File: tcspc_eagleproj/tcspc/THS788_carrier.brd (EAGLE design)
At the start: 50.8 x 38.1 mm, 46 parts, among them J1 BXE-040-01-F-D-A_BSE, U1 THS788

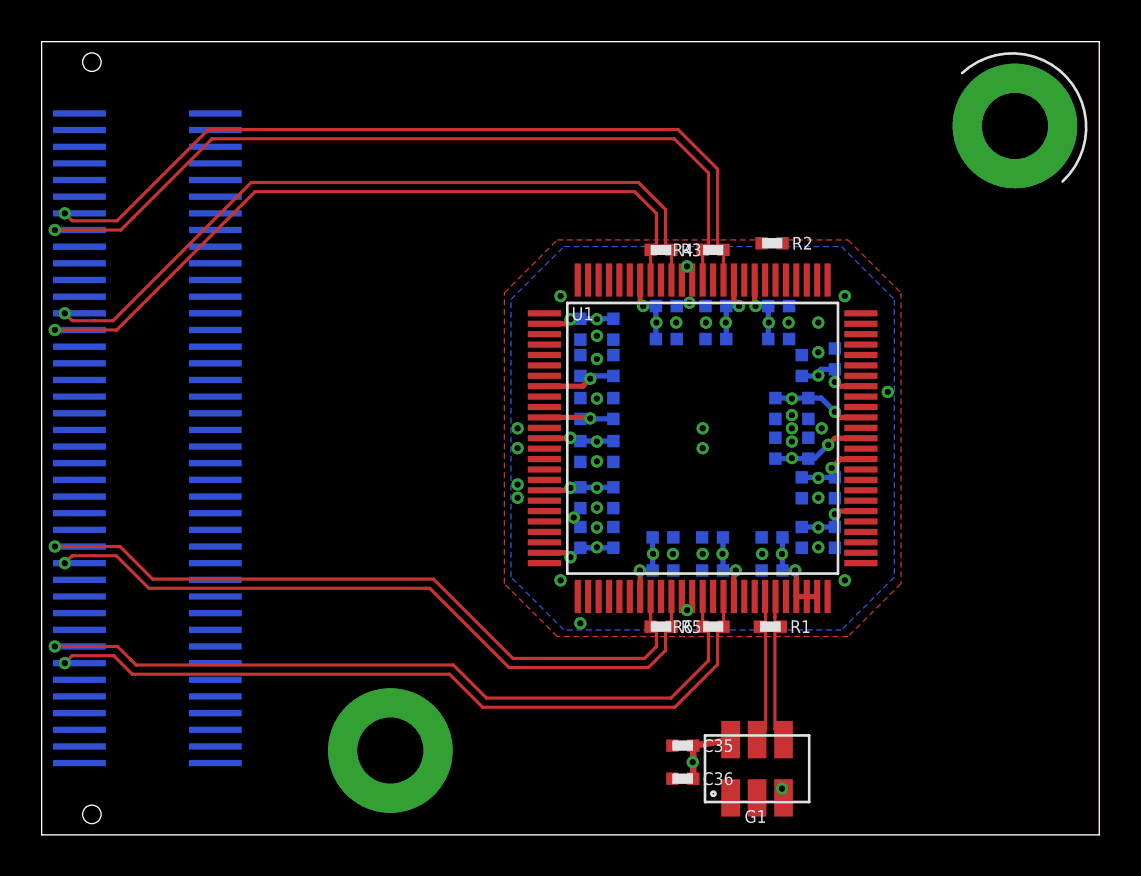
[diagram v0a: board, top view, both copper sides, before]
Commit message: Did a little more work on the THS788 carrier, routed a few more HS diff signals
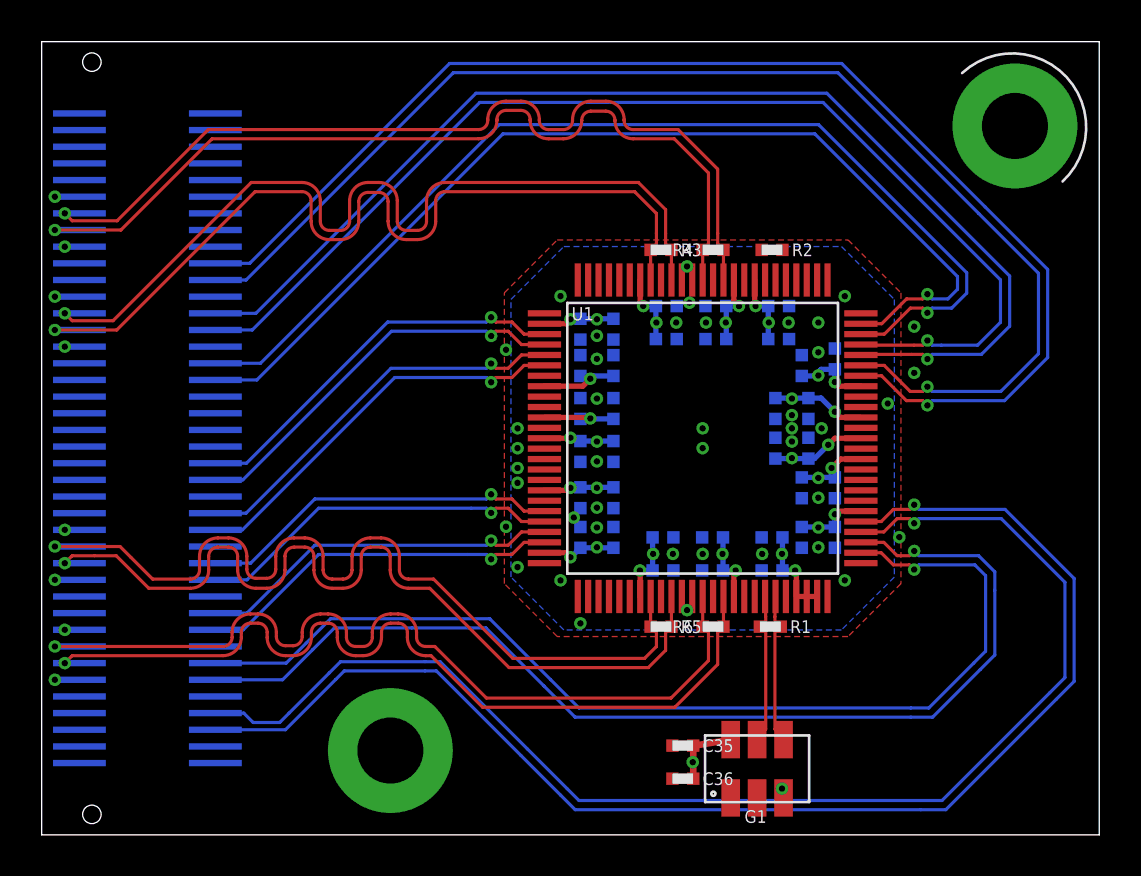
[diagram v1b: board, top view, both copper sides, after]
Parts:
- moved R2 0.32 mm to (35.1, 28.1)
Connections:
- removed net !RCLK_OUT: U1.44
- removed net !RDATA-A_OUT: U1.79
- removed net !RDATA-B_OUT: U1.48
- removed net !RDATA-C_OUT: U1.97
- removed net !RDATA-D_OUT: U1.28
- removed net !RSTROBE-A_OUT: U1.81
- removed net !RSTROBE-B_OUT: U1.46
- removed net !RSTROBE-C_OUT: U1.95
- removed net !RSTROBE-D_OUT: U1.30
- removed net !SYNC_IN: R2.1, U1.56
- removed net RCLK_OUT: U1.45
- removed net RDATA-A_OUT: U1.78
- removed net RDATA-B_OUT: U1.49
- removed net RDATA-C_OUT: U1.98
- removed net RDATA-D_OUT: U1.27
- removed net RSTROBE-A_OUT: U1.80
- removed net RSTROBE-B_OUT: U1.47
- removed net RSTROBE-C_OUT: U1.96
- removed net RSTROBE-D_OUT: U1.29
- removed net SYNC_IN: R2.2, U1.57
- new net RCLK_OUT_N: J1.19, U1.44
- new net RCLK_OUT_P: J1.21, U1.45
- new net RDATA-A_OUT_N: J1.45, U1.79
- new net RDATA-A_OUT_P: J1.43, U1.78
- new net RDATA-B_OUT_N: J1.31, U1.48
- new net RDATA-B_OUT_P: J1.33, U1.49
- new net RDATA-C_OUT_N: J1.61, U1.97
- new net RDATA-C_OUT_P: J1.63, U1.98
- new net RDATA-D_OUT_N: J1.69, U1.28
- new net RDATA-D_OUT_P: J1.67, U1.27
- new net RSTROBE-A_OUT_N: J1.51, U1.81
- new net RSTROBE-A_OUT_P: J1.49, U1.80
- new net RSTROBE-B_OUT_N: J1.25, U1.46
- new net RSTROBE-B_OUT_P: J1.27, U1.47
- new net RSTROBE-C_OUT_N: J1.55, U1.95
- new net RSTROBE-C_OUT_P: J1.57, U1.96
- new net RSTROBE-D_OUT_N: J1.75, U1.30
- new net RSTROBE-D_OUT_P: J1.73, U1.29
- new net SYNC_IN_N: J1.37, R2.1, U1.56
- new net SYNC_IN_P: J1.39, R2.2, U1.57
- net !HSTROBE_IN: now also J1.9
- net !RESET_IN: now also J1.11
- net GND: now also J1.12, J1.17, J1.18, J1.23, J1.24, J1.29, J1.3, J1.30, J1.35, J1.41, J1.47, J1.52, J1.53, J1.58, J1.59, J1.64, J1.65, J1.70, J1.71, J1.77
- net HCLK_IN: now also J1.7
- net HDATA_IN: now also J1.5
- net OT_ALRM_OUT: now also J1.15
- net TEMP_OUT: now also J1.13
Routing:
- net RSTROBE-D_OUT_N: track 0.00 -> 64.7 mm, vias 0 -> 1
- net RSTROBE-D_OUT_P: track 0.00 -> 63.5 mm, vias 0 -> 1
- net RCLK_OUT_N: track 0.00 -> 62.8 mm, vias 0 -> 1
- net RCLK_OUT_P: track 0.00 -> 61.5 mm, vias 0 -> 1
- net RSTROBE-B_OUT_N: track 0.00 -> 56.5 mm, vias 0 -> 1
- net RSTROBE-B_OUT_P: track 0.00 -> 55.2 mm, vias 0 -> 1
- net RDATA-D_OUT_N: track 0.00 -> 52.7 mm, vias 0 -> 1
- net RDATA-D_OUT_P: track 0.00 -> 51.0 mm, vias 0 -> 1
- net RDATA-B_OUT_N: track 0.00 -> 50.8 mm, vias 0 -> 1
- net RDATA-B_OUT_P: track 0.00 -> 49.5 mm, vias 0 -> 1
- net RSTROBE-A_OUT_N: track 0.00 -> 19.3 mm, vias 0 -> 1
- net RDATA-A_OUT_N: track 0.00 -> 19.2 mm, vias 0 -> 1
- net RSTROBE-A_OUT_P: track 0.00 -> 19.1 mm, vias 0 -> 1
- net RDATA-A_OUT_P: track 0.00 -> 19.0 mm, vias 0 -> 1
- net RDATA-C_OUT_P: track 0.00 -> 17.7 mm, vias 0 -> 1
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- added copper zone on layer 2, net GND
- added copper zone on layer 15, net PP_P3V3
- removed copper zone on layer 15, net GND
- removed copper zone on layer 2, net PP_P3V3
